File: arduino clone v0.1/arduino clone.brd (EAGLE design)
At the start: 86.3 x 27.6 mm, 47 parts, among them J203 ICSP HEADER, J402 FTDI Breakout Header, U101 ATMEGA328P_TQFP, U301 CH340G, Y101 16MHz, Y301 12MHz

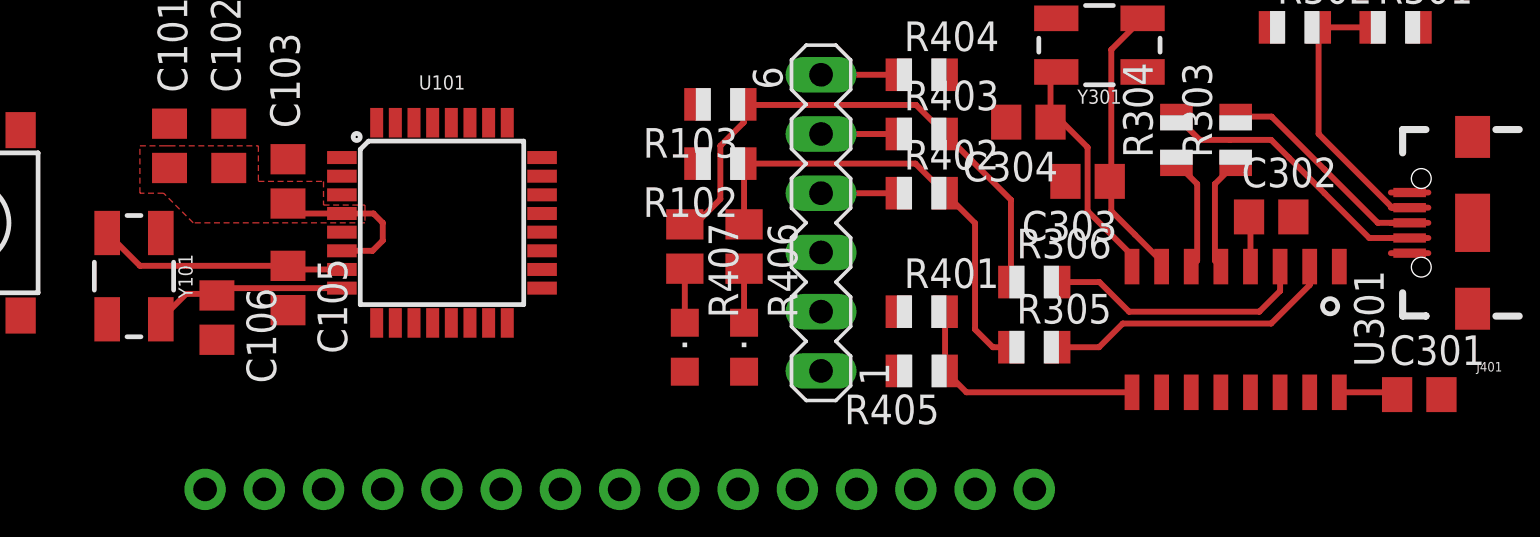
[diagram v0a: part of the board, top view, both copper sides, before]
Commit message: refine PP5V0_MCU shape
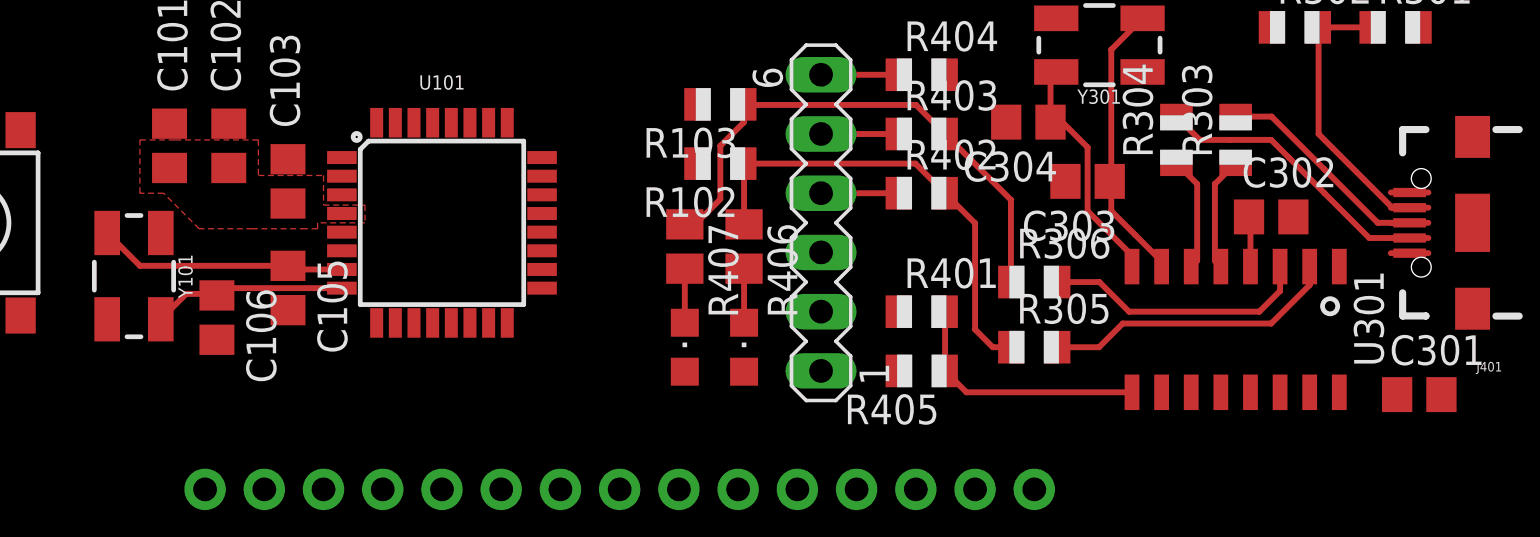
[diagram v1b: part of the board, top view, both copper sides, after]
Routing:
- net PP5V0_MCU: track 7.20 -> 0.00 mm
- net PP5V0_CH340G: track 2.52 -> 0.00 mm

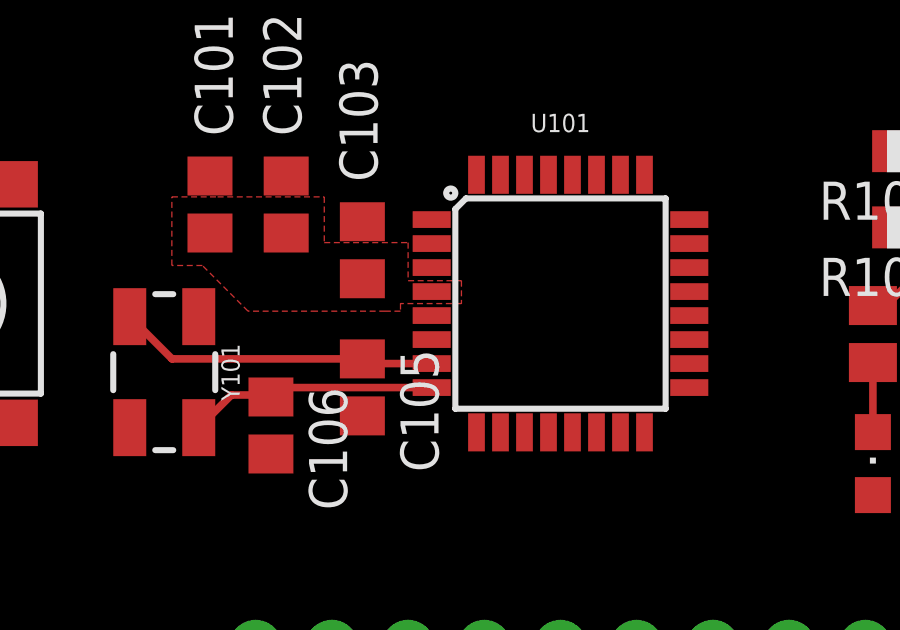
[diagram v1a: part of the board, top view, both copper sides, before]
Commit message: extend PP5V0_MCU shape to hit another nearby pin
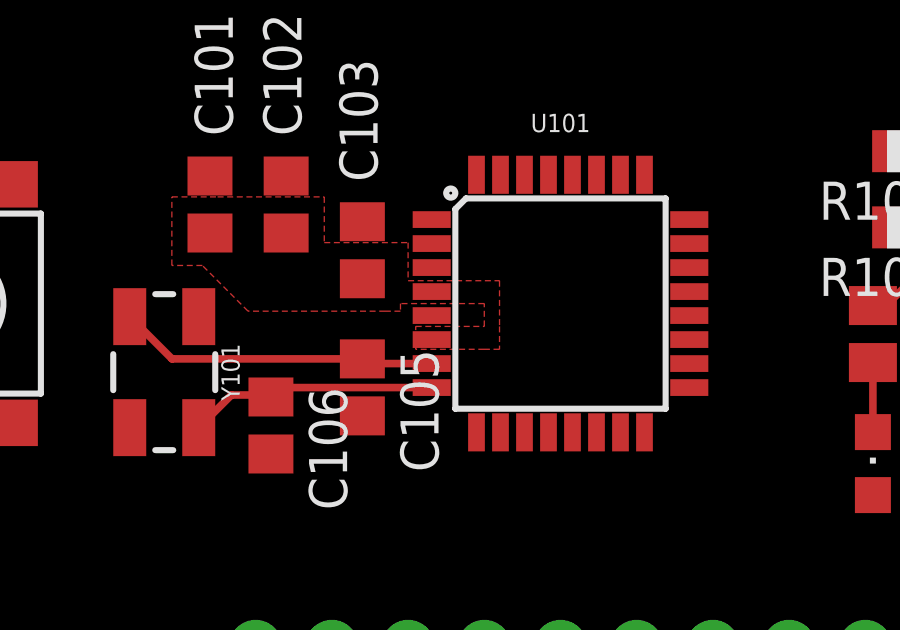
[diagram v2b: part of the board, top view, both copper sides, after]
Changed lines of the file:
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@@
 <vertex x="29.21" y="54.102"/>
 <vertex x="29.21" y="52.832"/>
-<vertex x="30.988" y="52.832"/>
-<vertex x="30.988" y="52.07"/>
+<vertex x="32.258" y="52.832"/>
+<vertex x="32.258" y="51.308"/>
+<vertex x="32.258" y="50.546"/>
+<vertex x="31.75" y="50.546"/>
+<vertex x="29.464" y="50.546"/>
+<vertex x="29.464" y="51.308"/>
+<vertex x="31.75" y="51.308"/>
+<vertex x="31.75" y="52.07"/>
 <vertex x="28.956" y="52.07"/>
 <vertex x="28.956" y="51.816"/>
@@
 <wire x1="38.5826" y1="50.07" x2="44.704" y2="45.686" width="0" layer="19" extent="1-1"/>
 <wire x1="29.9974" y1="50.87" x2="38.5826" y2="50.07" width="0" layer="19" extent="1-1"/>
-<wire x1="29.9974" y1="52.47" x2="29.9974" y2="50.87" width="0" layer="19" extent="1-1"/>
 <wire x1="-18.05" y1="56.896" x2="22.606" y2="54.422" width="0" layer="19" extent="1-1"/>
 <wire x1="-42.91" y1="41.91" x2="-18.05" y2="56.896" width="0" layer="19" extent="1-1"/>

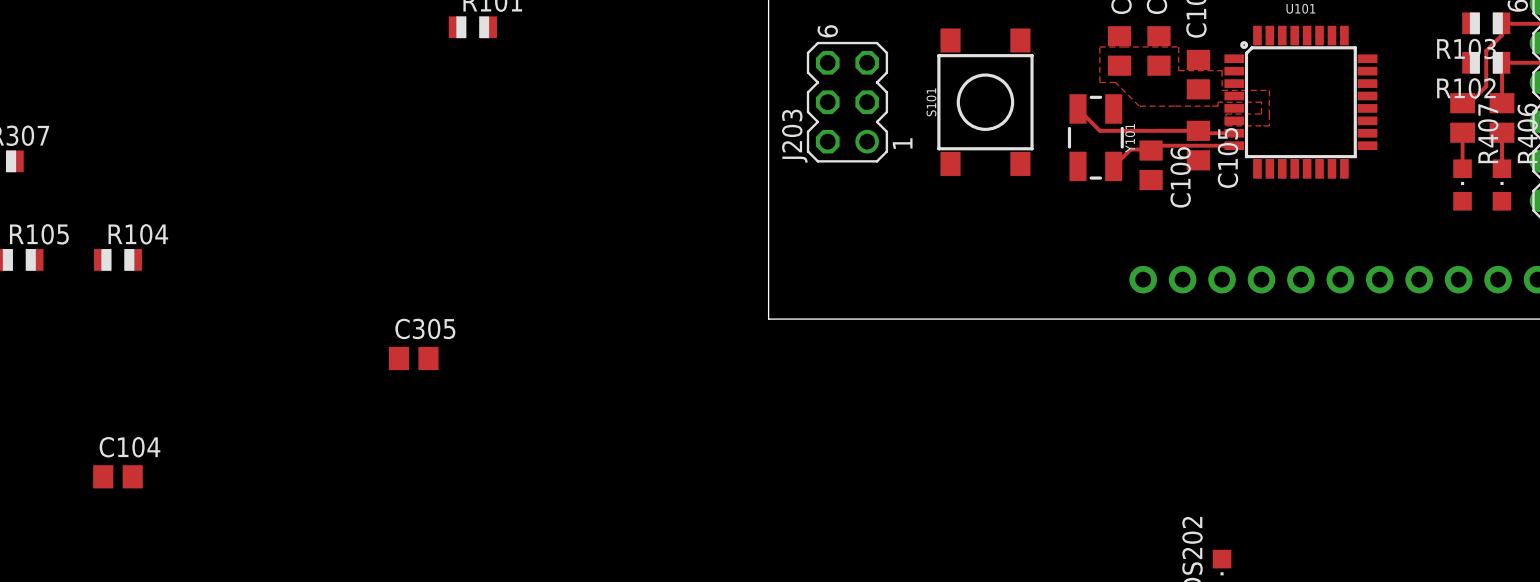
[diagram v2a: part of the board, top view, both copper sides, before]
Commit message: place and route decoupling cap C104
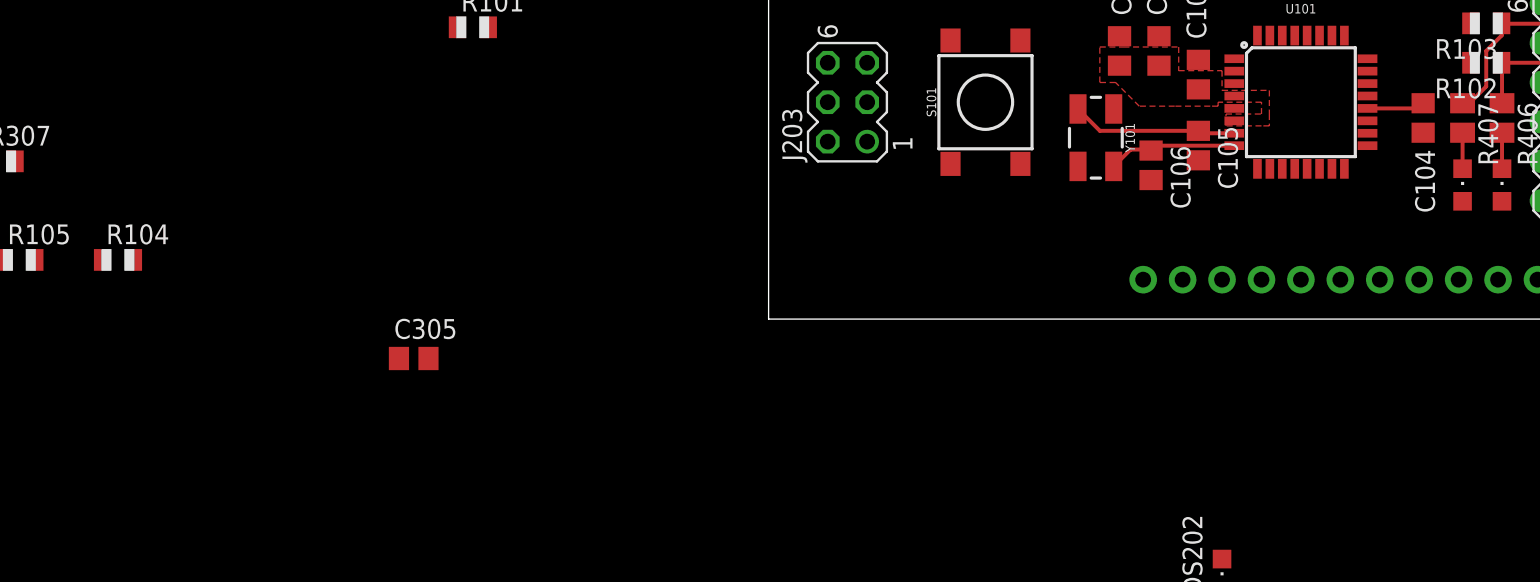
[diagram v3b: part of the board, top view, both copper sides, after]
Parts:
- moved C104 87.2 mm to (42.2, 51.1), turned to 270 degrees
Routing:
- net MCU_AREF: track 0.00 -> 3.72 mm
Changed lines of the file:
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@@
 <attribute name="VALUE" x="30.226" y="52.578" size="1.27" layer="27" rot="R90"/>
 </element>
-<element name="C104" library="rcl" library_urn="urn:adsk.eagle:library:334" package="C0805" package3d_urn="urn:adsk.eagle:package:23617/2" value="100nF" x="-41.91" y="27.94" smashed="yes">
-<attribute name="NAME" x="-43.18" y="29.21" size="1.27" layer="25"/>
-<attribute name="SPICEPREFIX" value="C" x="-41.91" y="27.94" size="1.778" layer="27" display="off"/>
-<attribute name="VALUE" x="-43.18" y="25.4" size="1.27" layer="27"/>
+<element name="C104" library="rcl" library_urn="urn:adsk.eagle:library:334" package="C0805" package3d_urn="urn:adsk.eagle:package:23617/2" value="100nF" x="42.164" y="51.054" smashed="yes" rot="R270">
+<attribute name="NAME" x="41.656" y="49.022" size="1.27" layer="25" rot="R270"/>
+<attribute name="SPICEPREFIX" value="C" x="42.164" y="51.054" size="1.778" layer="27" rot="R270" display="off"/>
 </element>
 <element name="C105" library="rcl" library_urn="urn:adsk.eagle:library:334" package="C0805" package3d_urn="urn:adsk.eagle:package:23617/2" value="22pF" x="27.686" y="49.276" smashed="yes" rot="R270">
@@
 <wire x1="31.75" y1="40.64" x2="27.686" y2="48.326" width="0" layer="19" extent="1-1"/>
 <wire x1="3.81" y1="54.61" x2="16.22" y2="56.045" width="0" layer="19" extent="1-1"/>
-<wire x1="-40.96" y1="27.94" x2="3.81" y2="54.61" width="0" layer="19" extent="1-1"/>
-<wire x1="-41.59" y1="15.24" x2="-40.96" y2="27.94" width="0" layer="19" extent="1-1"/>
+<wire x1="42.164" y1="50.104" x2="3.81" y2="54.61" width="0" layer="19" extent="1-1"/>
+<wire x1="-41.59" y1="15.24" x2="42.164" y2="50.104" width="0" layer="19" extent="1-1"/>
 <wire x1="-39.05" y1="7.62" x2="-41.59" y2="15.24" width="0" layer="19" extent="1-1"/>
-<wire x1="-56.88" y1="48.26" x2="-40.96" y2="27.94" width="0" layer="19" extent="1-1"/>
+<wire x1="-56.88" y1="48.26" x2="42.164" y2="50.104" width="0" layer="19" extent="1-1"/>
 </signal>
 <signal name="MCU_RESET">
@@
 <contactref element="U101" pad="20"/>
 <contactref element="J202" pad="13"/>
-<wire x1="38.5826" y1="51.67" x2="54.61" y2="63.5" width="0" layer="19" extent="1-1"/>
-<wire x1="-42.86" y1="27.94" x2="38.5826" y2="51.67" width="0" layer="19" extent="1-1"/>
+<wire x1="38.5826" y1="51.67" x2="41.83" y2="51.67" width="0.254" layer="1"/>
+<wire x1="41.83" y1="51.67" x2="42.164" y2="52.004" width="0.1524" layer="1"/>
+<wire x1="42.164" y1="52.004" x2="54.61" y2="63.5" width="0" layer="19" extent="1-1"/>
 </signal>
 <signal name="MCU_D1">

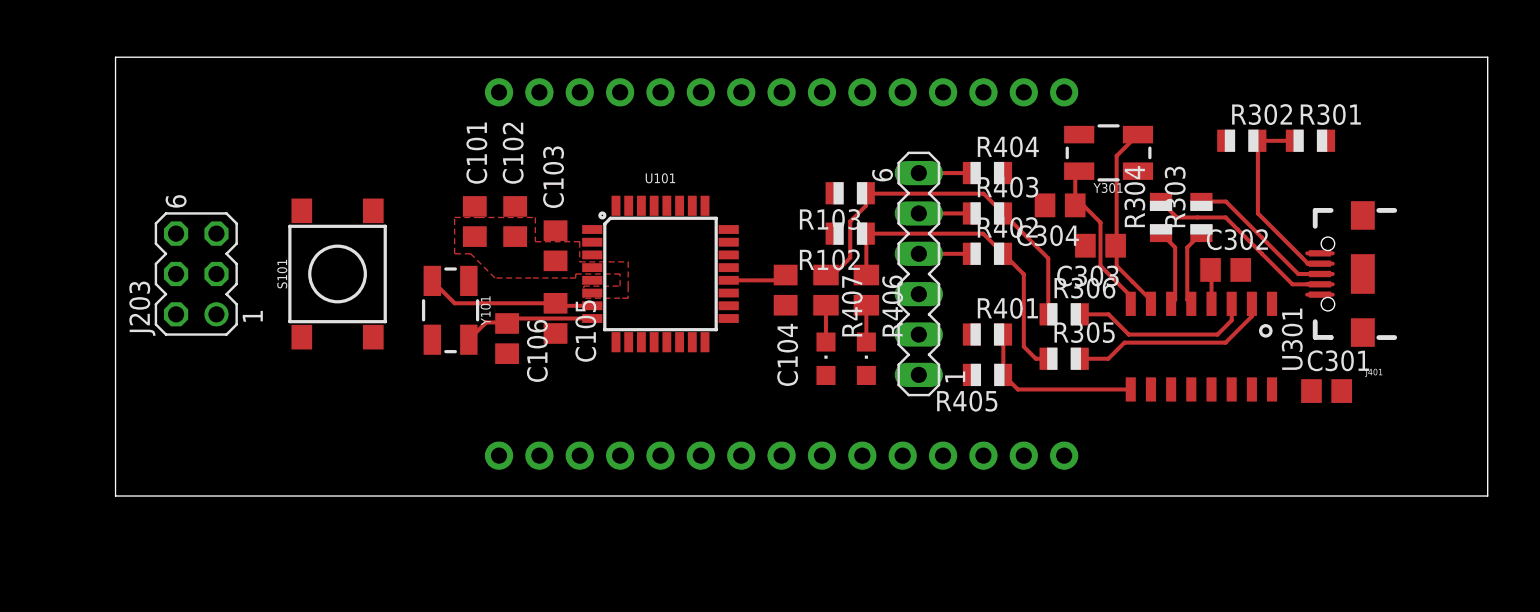
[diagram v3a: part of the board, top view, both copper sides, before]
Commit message: add top gnd place
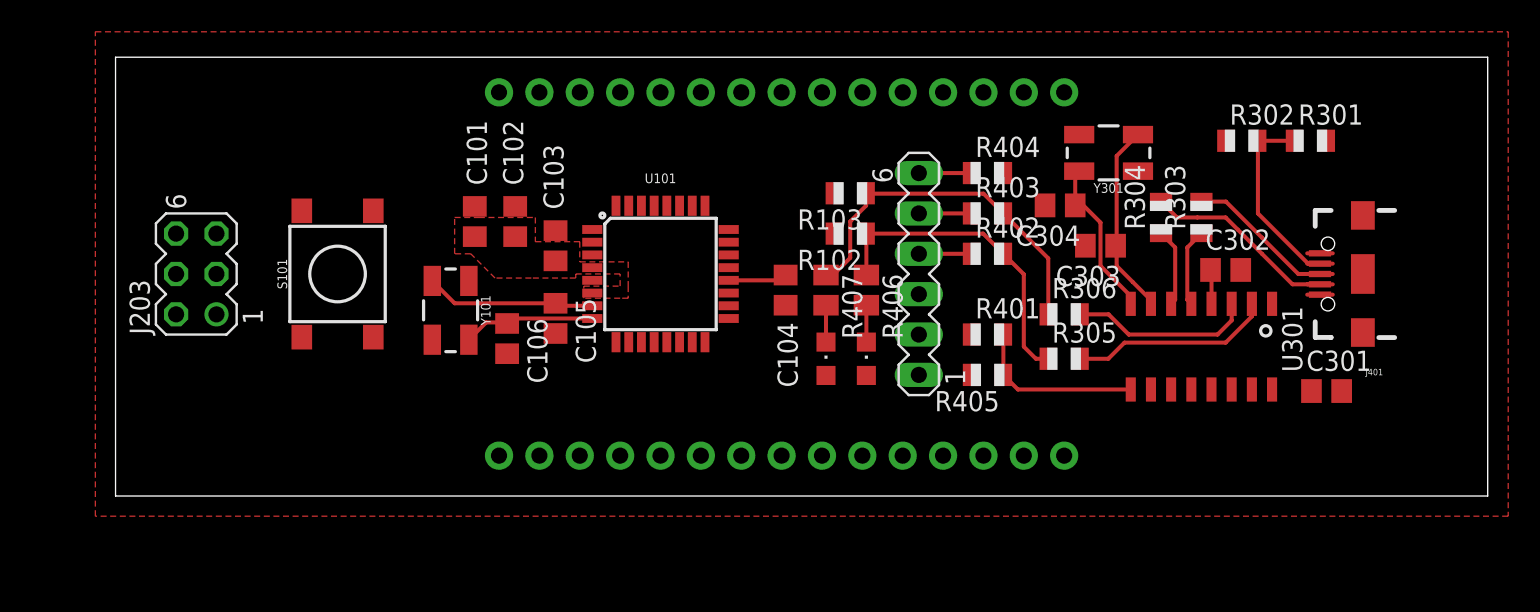
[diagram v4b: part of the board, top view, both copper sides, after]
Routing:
- added copper zone on layer 1, net GND
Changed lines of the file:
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@@
 <setting verticaltext="up"/>
 </settings>
-<grid distance="10" unitdist="mil" unit="mil" style="lines" multiple="1" display="yes" altdistance="5" altunitdist="mil" altunit="mil"/>
+<grid distance="50" unitdist="mil" unit="mil" style="lines" multiple="1" display="yes" altdistance="5" altunitdist="mil" altunit="mil"/>
 <layers>
 <layer number="1" name="Top" color="4" fill="1" visible="yes" active="yes"/>
@@
 <contactref element="R201" pad="1"/>
 <contactref element="R202" pad="1"/>
-<wire x1="70.8" y1="52.324" x2="69.866" y2="60.452" width="0" layer="19" extent="1-1"/>
-<wire x1="72.771" y1="50.193" x2="70.8" y2="52.324" width="0" layer="19" extent="1-1"/>
-<wire x1="75.786" y1="53.37" x2="72.771" y2="50.193" width="0" layer="19" extent="1-1"/>
-<wire x1="77.15" y1="44.704" x2="72.771" y2="50.193" width="0" layer="19" extent="1-1"/>
-<wire x1="61.026" y1="53.848" x2="70.8" y2="52.324" width="0" layer="19" extent="1-1"/>
-<wire x1="58.486" y1="56.388" x2="61.026" y2="53.848" width="0" layer="19" extent="1-1"/>
-<wire x1="53.864" y1="45.72" x2="61.026" y2="53.848" width="0" layer="19" extent="1-1"/>
-<wire x1="50.546" y1="45.72" x2="53.864" y2="45.72" width="0" layer="19" extent="1-1"/>
-<wire x1="38.5826" y1="52.47" x2="50.546" y2="45.72" width="0" layer="19" extent="1-1"/>
-<wire x1="29.9974" y1="51.67" x2="38.5826" y2="52.47" width="0" layer="19" extent="1-1"/>
-<wire x1="29.9974" y1="53.27" x2="29.9974" y2="51.67" width="0" layer="19" extent="1-1"/>
-<wire x1="27.686" y1="54.798" x2="29.9974" y2="53.27" width="0" layer="19" extent="1-1"/>
-<wire x1="25.146" y1="56.322" x2="27.686" y2="54.798" width="0" layer="19" extent="1-1"/>
-<wire x1="22.606" y1="56.322" x2="25.146" y2="56.322" width="0" layer="19" extent="1-1"/>
-<wire x1="27.686" y1="48.326" x2="29.9974" y2="51.67" width="0" layer="19" extent="1-1"/>
-<wire x1="24.638" y1="47.056" x2="27.686" y2="48.326" width="0" layer="19" extent="1-1"/>
-<wire x1="16.22" y1="56.045" x2="22.606" y2="56.322" width="0" layer="19" extent="1-1"/>
-<wire x1="26.67" y1="63.5" x2="25.146" y2="56.322" width="0" layer="19" extent="1-1"/>
-<wire x1="31.75" y1="40.64" x2="27.686" y2="48.326" width="0" layer="19" extent="1-1"/>
-<wire x1="3.81" y1="54.61" x2="16.22" y2="56.045" width="0" layer="19" extent="1-1"/>
-<wire x1="42.164" y1="50.104" x2="3.81" y2="54.61" width="0" layer="19" extent="1-1"/>
-<wire x1="-41.59" y1="15.24" x2="42.164" y2="50.104" width="0" layer="19" extent="1-1"/>
+<polygon width="0.0762" layer="1" rank="6">
+<vertex x="-1.27" y="67.31"/>
+<vertex x="87.63" y="67.31"/>
+<vertex x="87.63" y="36.83"/>
+<vertex x="-1.27" y="36.83"/>
+</polygon>
+<wire x1="72.771" y1="50.193" x2="75.786" y2="53.37" width="0" layer="19" extent="1-1"/>
+<wire x1="29.9974" y1="51.67" x2="29.9974" y2="53.27" width="0" layer="19" extent="1-1"/>
+<wire x1="-41.59" y1="15.24" x2="3.81" y2="54.61" width="0" layer="19" extent="1-1"/>
 <wire x1="-39.05" y1="7.62" x2="-41.59" y2="15.24" width="0" layer="19" extent="1-1"/>
-<wire x1="-56.88" y1="48.26" x2="42.164" y2="50.104" width="0" layer="19" extent="1-1"/>
+<wire x1="-56.88" y1="48.26" x2="-41.59" y2="15.24" width="0" layer="19" extent="1-1"/>
 </signal>
 <signal name="MCU_RESET">
